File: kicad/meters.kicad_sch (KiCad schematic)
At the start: 38 parts, among them U7 NE5532, U8 LM3914, U9 LM3915

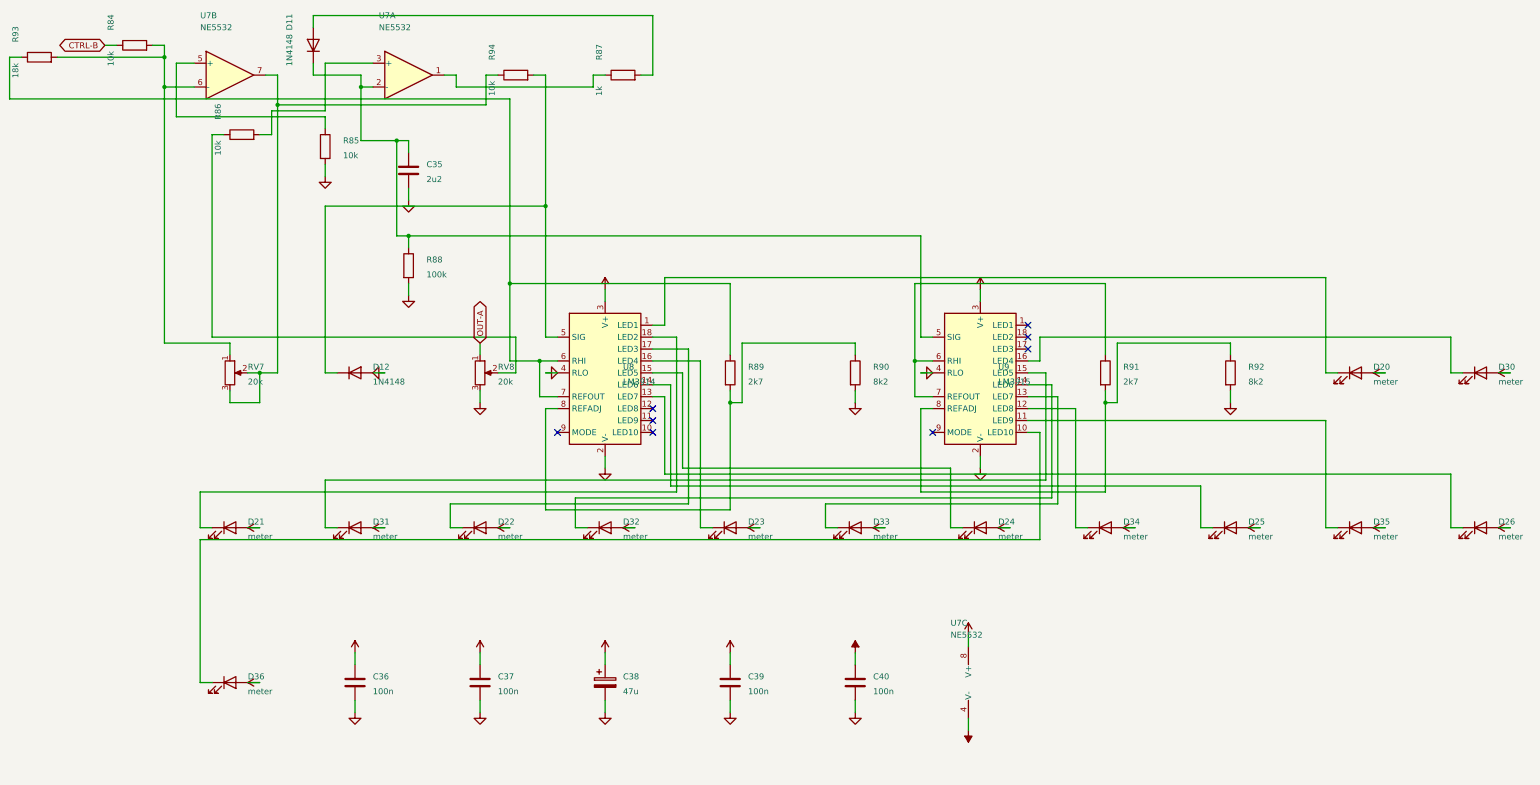
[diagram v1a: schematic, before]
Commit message: Add reorganised schematic to split files.
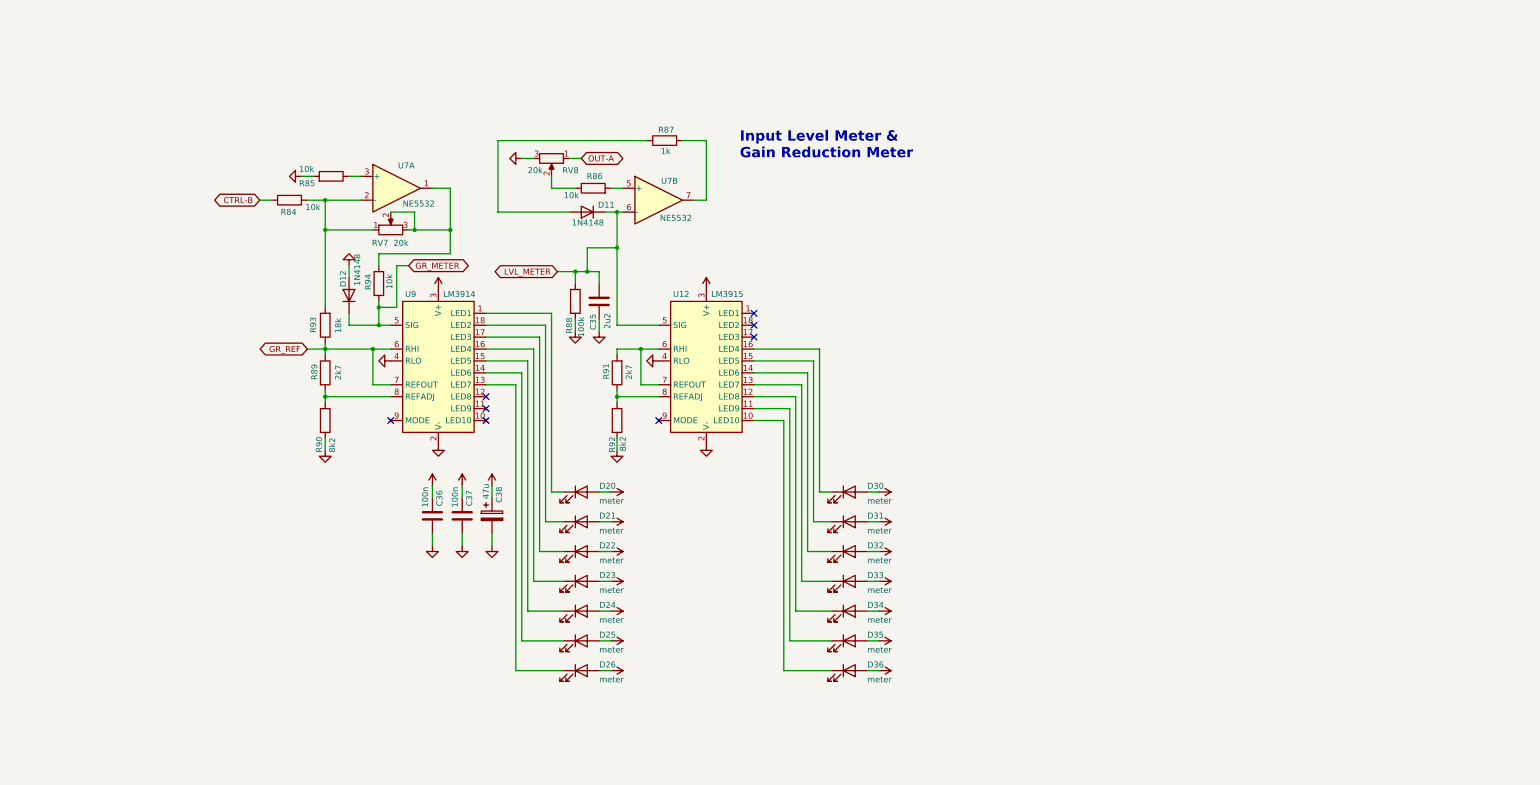
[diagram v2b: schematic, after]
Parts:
- removed C39, C40: 100n, Capacitor_THT:C_Disc_D5.0mm_W2.5mm_P5.00mm, symbol Device:C
- removed unit 3 of U7
- removed U8: LM3914, Package_DIP:DIP-18_W7.62mm, symbol Driver_LED:LM3914N
- added U12: LM3915, Package_DIP:DIP-18_W7.62mm, symbol Driver_LED:LM3914N
- C36, C37, C38, D20, D21, D22, D23, D24, D25, D26, D30, D31, D32, D33, D34, D35, D36, R89, R90, R91, R92: now left out of the parts list
- U7: footprint Package_DIP:DIP-8_W7.62mm -> Package_DIP:DIP-8_W7.62mm_Socket
- U9: value LM3915 -> LM3914; now left out of the parts list
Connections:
- net +16V: now also U12.3 (V+)
- net AGND: now also U12.2 (V-), U12.4 (RLO)
- net at U9.1 (LED1): now also D20.1 (K)
- net at D36.1 (K): now also U12.10 (LED10); no longer U9.10 (LED10)
- net at D35.1 (K): now also U12.11 (LED9); no longer U9.11 (LED9)
- net at D34.1 (K): now also U12.12 (LED8); no longer U9.12 (LED8)
- net at D33.1 (K): now also U12.13 (LED7); no longer U9.13 (LED7)
- net at U9.14 (LED6): now also D25.1 (K); no longer D32.1 (K)
- net at U9.15 (LED5): now also D24.1 (K); no longer D31.1 (K)
- net at D30.1 (K): now also U12.16 (LED4); no longer U9.16 (LED4)
- net at U9.17 (LED3): now also D22.1 (K)
- net at U9.18 (LED2): now also D21.1 (K)
- net LVL_METER: now reaches C35.1, D11.1 (K), R88.1
- net LVL_METER: now also U7.6 (-), U12.5 (SIG); no longer U7.2 (-), U9.5 (SIG)
- net GR_REF: now reaches U9.6 (RHI), U9.7 (REFOUT)
- net GR_REF: now also R89.1, R93.1; no longer R91.1
- net at D23.1 (K): now also U9.16 (LED4)
- net at R84.2, R93.2, RV7.1: now also U7.2 (-); no longer U7.6 (-)
- net at U7.1: now also R94.2, RV7.2, RV7.3; no longer R87.1
- net at R86.2: now also U7.5 (+); no longer U7.3 (+)
- net at D26.1 (K): now also U9.13 (LED7)
- net GR_METER: now reaches D12.1 (K)
- net GR_METER: now also R94.1, U9.5 (SIG); no longer R94.2
- net at R89.2, R90.1: now also U9.8 (REFADJ)
- net at D11.2 (A): now also R87.1; no longer R87.2
- net at R85.1: now also U7.3 (+); no longer U7.5 (+)
- new net: R91.1, R92.1, U12.8 (REFADJ)
- new net: D32.1 (K), U12.14 (LED6)
- new net: D31.1 (K), U12.15 (LED5)
- new net: R91.2, U12.6 (RHI), U12.7 (REFOUT)
- new net: R87.2, U7.7
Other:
- note added: "Input Level Meter & Gain Reduction Meter"

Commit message: Match the split sheets' chip references to the board (#4)
Pasting the board schematic into the split sheets renumbered five units:
the VCA recovery amp was U4B (board U1B), the sidechain TL072 was U10
(board U4), U4's power unit was U10, U7's power unit was U11, and the
LM3915 was U12 (board U10). They now carry the board's references, so
the split sheets and compressor_with_pcb have the same 167 parts and the
same 119 nets.
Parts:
- renumbered U12 to U10
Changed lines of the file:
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@@
 		(in_pos_files yes)
 		(dnp no)
-		(property "Reference" "U12"
+		(property "Reference" "U10"
 			(at 168.148 86.106 0)
 			(show_name no)
@@
 			(project "UTS Mini Mixing Desk - Compressor"
 				(path "/fdeae63a-37f5-58fb-b342-cb68d8a6bfbc/c0164a91-c3d2-5b1a-8cc9-b3c638b0e13a"
-					(reference "U12")
+					(reference "U10")
 					(unit 1)
 				)

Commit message: Fit real film capacitors on the main board and use Altronics pots for RV5/RV6
RV5 (ATTACK) goes 4k7 -> 10k and RV6 (RELEASE) 500k -> 1M, the nearest
Altronics 9 mm values (R1946, R1950), on the split sheets, both boards
and design.py; the Sim.Params follow (R=10000, R=1e+06).

C5, C8, C9, C10, C14, C15 and C35 were drawn as 7 x 2.5 mm on 5 mm, which
no 2.2-10 uF film part fits. They now use stock KiCad footprints for
in-stock element14 parts:
  10 uF  C5 C8 C15  TDK B32562H1106K000   C_Rect_L16.5mm_W11.8mm_P15.00mm_MKT
  4.7 uF C9 C10     TDK B32562H1475K000   C_Rect_L16.5mm_W7.3mm_P15.00mm_MKT
  2.2 uF C14 C35    KEMET MMK5225K63J06L4 C_Rect_L7.2mm_W7.2mm_P5.00mm_FKS2...

To make room, small parts were re-placed by script (the caps near their
old spots, displaced parts re-homed, then same-footprint parts swapped to
cut wire length; transistors, ICs, connectors and trimmers did not move)
and the main board was re-routed with Freerouting, keeping the original
card-finger stubs. DRC 0 errors, 0 unconnected, schematic parity clean;
ERC 0 errors. The BOM names the element14 parts.
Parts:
- C35: footprint Capacitor_THT:C_Rect_L7.0mm_W2.5mm_P5.00mm -> Capacitor_THT:C_Rect_L7.2mm_W7.2mm_P5.00mm_FKS2_FKP2_MKS2_MKP2
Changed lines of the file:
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@@
 			)
 		)
-		(property "Footprint" "Capacitor_THT:C_Rect_L7.0mm_W2.5mm_P5.00mm"
+		(property "Footprint" "Capacitor_THT:C_Rect_L7.2mm_W7.2mm_P5.00mm_FKS2_FKP2_MKS2_MKP2"
 			(at 152.4 87.63 0)
 			(hide yes)

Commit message: Swap the level meter's LM3915 for an LM3914 on outputs 1-7
Nobody stocks the LM3915, so U10 becomes a second LM3914. The LEDs move
to outputs 1-7 and outputs 8-10 join the top LED, giving a 17 dB scale
with no added parts. Front board LVL tracks re-routed; BOM regenerated.
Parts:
- U10: value LM3915 -> LM3914
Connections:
- net LVLL6: now reaches D35.1 (K)
- net LVLL6: now also U10.14 (LED6); no longer U10.11 (LED9)
- net LVLL1: now reaches D30.1 (K)
- net LVLL1: now also U10.1 (LED1); no longer U10.16 (LED4)
- net LVLL7: now reaches D36.1 (K), U10.10 (LED10)
- net LVLL7: now also U10.11 (LED9), U10.12 (LED8), U10.13 (LED7)
- net LVLL5: now reaches D34.1 (K)
- net LVLL5: now also U10.15 (LED5); no longer U10.12 (LED8)
- net LVLL4: now reaches D33.1 (K)
- net LVLL4: now also U10.16 (LED4); no longer U10.13 (LED7)
- net LVLL3: now reaches D32.1 (K)
- net LVLL3: now also U10.17 (LED3); no longer U10.14 (LED6)
- net LVLL2: now reaches D31.1 (K)
- net LVLL2: now also U10.18 (LED2); no longer U10.15 (LED5)
- no-connect marks 8 -> 5
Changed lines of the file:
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@@
 	)
 	(no_connect
-		(at 185.42 92.71)
-	)
-	(no_connect
 		(at 107.95 113.03)
 	)
@@
 	)
 	(no_connect
-		(at 185.42 90.17)
-	)
-	(no_connect
 		(at 128.27 110.49)
 	)
-	(no_connect
-		(at 185.42 95.25)
-	)
 	(wire
 		(pts
@@
 	(wire
 		(pts
-			(xy 185.42 107.95) (xy 194.31 107.95)
-		)
-		(stroke
-			(width 0)
-			(type default)
-		)
-	)
-	(wire
-		(pts
 			(xy 99.06 92.71) (xy 105.41 92.71)
 		)
@@
 	(wire
 		(pts
-			(xy 185.42 102.87) (xy 196.85 102.87)
-		)
-		(stroke
-			(width 0)
-			(type default)
-		)
-	)
-	(wire
-		(pts
 			(xy 152.4 128.27) (xy 154.94 128.27)
 		)
@@
 	(wire
 		(pts
-			(xy 191.77 113.03) (xy 185.42 113.03)
-		)
-		(stroke
-			(width 0)
-			(type default)
-		)
-	)
-	(wire
-		(pts
 			(xy 93.98 97.79) (xy 104.14 97.79)
 		)
@@
 	(wire
 		(pts
-			(xy 185.42 97.79) (xy 199.39 97.79)
-		)
-		(stroke
-			(width 0)
-			(type default)
-		)
-	)
-	(wire
-		(pts
 			(xy 107.95 107.95) (xy 93.98 107.95)
 		)
@@
 	(wire
 		(pts
-			(xy 185.42 105.41) (xy 195.58 105.41)
-		)
-		(stroke
-			(width 0)
-			(type default)
-		)
-	)
-	(wire
-		(pts
-			(xy 185.42 110.49) (xy 193.04 110.49)
-		)
-		(stroke
-			(width 0)
-			(type default)
-		)
-	)
-	(wire
-		(pts
 			(xy 152.4 81.28) (xy 152.4 83.82)
 		)
@@
 	(wire
 		(pts
-			(xy 185.42 100.33) (xy 198.12 100.33)
-		)
-		(stroke
-			(width 0)
-			(type default)
-		)
-	)
-	(wire
-		(pts
 			(xy 90.17 66.04) (xy 93.98 66.04)
 		)
@@
 			)
 		)
-		(property "Value" "LM3915"
+		(property "Value" "LM3914"
 			(at 176.276 86.106 0)
 			(show_name no)
@@
 		)
 	)
+	(label "LVLL1"
+		(at 199.39 97.79 0)
+		(fields_autoplaced yes)
+		(effects
+			(font
+				(size 1.27 1.27)
+			)
+			(justify left bottom)
+		)
+	)
+	(label "LVLL2"
+		(at 198.12 100.33 0)
+		(fields_autoplaced yes)
+		(effects
+			(font
+				(size 1.27 1.27)
+			)
+			(justify left bottom)
+		)
+	)
+	(label "LVLL3"
+		(at 196.85 102.87 0)
+		(fields_autoplaced yes)
+		(effects
+			(font
+				(size 1.27 1.27)
+			)
+			(justify left bottom)
+		)
+	)
+	(label "LVLL4"
+		(at 195.58 105.41 0)
+		(fields_autoplaced yes)
+		(effects
+			(font
+				(size 1.27 1.27)
+			)
+			(justify left bottom)
+		)
+	)
+	(label "LVLL5"
+		(at 194.31 107.95 0)
+		(fields_autoplaced yes)
+		(effects
+			(font
+				(size 1.27 1.27)
+			)
+			(justify left bottom)
+		)
+	)
+	(label "LVLL6"
+		(at 193.04 110.49 0)
+		(fields_autoplaced yes)
+		(effects
+			(font
+				(size 1.27 1.27)
+			)
+			(justify left bottom)
+		)
+	)
+	(label "LVLL7"
+		(at 191.77 113.03 0)
+		(fields_autoplaced yes)
+		(effects
+			(font
+				(size 1.27 1.27)
+			)
+			(justify left bottom)
+		)
+	)
+	(wire
+		(pts
+			(xy 185.42 113.03) (xy 187.96 113.03)
+		)
+		(stroke
+			(width 0)
+			(type default)
+		)
+	)
+	(label "LVLL7"
+		(at 187.96 113.03 0)
+		(fields_autoplaced yes)
+		(effects
+			(font
+				(size 1.27 1.27)
+			)
+			(justify left bottom)
+		)
+	)
+	(wire
+		(pts
+			(xy 185.42 110.49) (xy 187.96 110.49)
+		)
+		(stroke
+			(width 0)
+			(type default)
+		)
+	)
+	(label "LVLL7"
+		(at 187.96 110.49 0)
+		(fields_autoplaced yes)
+		(effects
+			(font
+				(size 1.27 1.27)
+			)
+			(justify left bottom)
+		)
+	)
+	(wire
+		(pts
+			(xy 185.42 107.95) (xy 187.96 107.95)
+		)
+		(stroke
+			(width 0)
+			(type default)
+		)
+	)
+	(label "LVLL7"
+		(at 187.96 107.95 0)
+		(fields_autoplaced yes)
+		(effects
+			(font
+				(size 1.27 1.27)
+			)
+			(justify left bottom)
+		)
+	)
+	(wire
+		(pts
+			(xy 185.42 105.41) (xy 187.96 105.41)
+		)
+		(stroke
+			(width 0)
+			(type default)
+		)
+	)
+	(label "LVLL7"
+		(at 187.96 105.41 0)
+		(fields_autoplaced yes)
+		(effects
+			(font
+				(size 1.27 1.27)
+			)
+			(justify left bottom)
+		)
+	)
+	(wire
+		(pts
+			(xy 185.42 102.87) (xy 187.96 102.87)
+		)
+		(stroke
+			(width 0)
+			(type default)
+		)
+	)
+	(label "LVLL6"
+		(at 187.96 102.87 0)
+		(fields_autoplaced yes)
+		(effects
+			(font
+				(size 1.27 1.27)
+			)
+			(justify left bottom)
+		)
+	)
+	(wire
+		(pts
+			(xy 185.42 100.33) (xy 187.96 100.33)
+		)
+		(stroke
+			(width 0)
+			(type default)
+		)
+	)
+	(label "LVLL5"
+		(at 187.96 100.33 0)
+		(fields_autoplaced yes)
+		(effects
+			(font
+				(size 1.27 1.27)
+			)
+			(justify left bottom)
+		)
+	)
+	(wire
+		(pts
+			(xy 185.42 97.79) (xy 187.96 97.79)
+		)
+		(stroke
+			(width 0)
+			(type default)
+		)
+	)
+	(label "LVLL4"
+		(at 187.96 97.79 0)
+		(fields_autoplaced yes)
+		(effects
+			(font
+				(size 1.27 1.27)
+			)
+			(justify left bottom)
+		)
+	)
+	(wire
+		(pts
+			(xy 185.42 95.25) (xy 187.96 95.25)
+		)
+		(stroke
+			(width 0)
+			(type default)
+		)
+	)
+	(label "LVLL3"
+		(at 187.96 95.25 0)
+		(fields_autoplaced yes)
+		(effects
+			(font
+				(size 1.27 1.27)
+			)
+			(justify left bottom)
+		)
+	)
+	(wire
+		(pts
+			(xy 185.42 92.71) (xy 187.96 92.71)
+		)
+		(stroke
+			(width 0)
+			(type default)
+		)
+	)
+	(label "LVLL2"
+		(at 187.96 92.71 0)
+		(fields_autoplaced yes)
+		(effects
+			(font
+				(size 1.27 1.27)
+			)
+			(justify left bottom)
+		)
+	)
+	(wire
+		(pts
+			(xy 185.42 90.17) (xy 187.96 90.17)
+		)
+		(stroke
+			(width 0)
+			(type default)
+		)
+	)
+	(label "LVLL1"
+		(at 187.96 90.17 0)
+		(fields_autoplaced yes)
+		(effects
+			(font
+				(size 1.27 1.27)
+			)
+			(justify left bottom)
+		)
+	)

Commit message: Give both meters ten LEDs and simulate them
Adds D27-D29 (GR outputs 8-10) and D37-D39 (LVL outputs 8-10) on all three
schematics. The front board's meter columns move to a 3.0 mm pitch with
LVL output 10 at the top; R90/R92 move to a 7.62 mm footprint and C38
turns to clear the LEDs; the affected nets were re-routed. R92 becomes 4k7
so RV8 can set the top LED at +18 dBu. The panel gets the six extra holes.
The LM3914 sim model now has its comparators and LED current sinks, and
tools/sim/meters.py simulates both meters.
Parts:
- added D27, D28, D29, D37, D38, D39: meter, LED_THT:LED_D2.0mm_W4.0mm_H2.8mm_FlatTop, symbol Device:LED
- R90: footprint Resistor_THT:R_Axial_DIN0207_L6.3mm_D2.5mm_P10.16mm_Horizontal -> Resistor_THT:R_Axial_DIN0207_L6.3mm_D2.5mm_P7.62mm_Horizontal
- R92: value 8k2 -> 4k7; footprint Resistor_THT:R_Axial_DIN0207_L6.3mm_D2.5mm_P10.16mm_Horizontal -> Resistor_THT:R_Axial_DIN0207_L6.3mm_D2.5mm_P7.62mm_Horizontal
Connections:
- net +16V: now also D27.2 (A), D28.2 (A), D29.2 (A), D37.2 (A), D38.2 (A), D39.2 (A)
- net LVLL7: no longer U10.10 (LED10), U10.11 (LED9), U10.12 (LED8)
- net GRL10: now reaches U9.10 (LED10)
- net GRL10: now also D29.1 (K)
- net GRL9: now reaches U9.11 (LED9)
- net GRL9: now also D28.1 (K)
- net GRL8: now reaches U9.12 (LED8)
- net GRL8: now also D27.1 (K)
- new net LVLL10: D39.1 (K), U10.10 (LED10)
- new net LVLL8: D37.1 (K), U10.12 (LED8)
- new net LVLL9: D38.1 (K), U10.11 (LED9)
- no-connect marks 5 -> 2
